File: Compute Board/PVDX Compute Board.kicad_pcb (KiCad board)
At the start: 2 copper layers, 82.5 x 82.5 mm, 84 parts, among them IC1 MCP1603-330I_MC, IC2 MCP1603-180I_MC, J1 USB_C_Receptacle_USB2.0_14P, J2 FTSH-105-01-L-DV-007-K, J3 Conn_01x02, J4 Conn_02x06_Top_Bottom, J5 Conn_02x08_Counter_Clockwise, J6 Conn_01x06, J7 Conn_01x07, J8 Conn_01x05, J9 Conn_01x08, U1 EM008LX, U10 Sen-Z-f, U11 SAMD51, U2 EM008LX, U3 EM008LX, U4 TXS0108EPW, U5 TXS0108EPW, U6 SCH16T-K01-1, U7 MagI2C, U8 Sen-XY-f, U9 Sen-XY-f

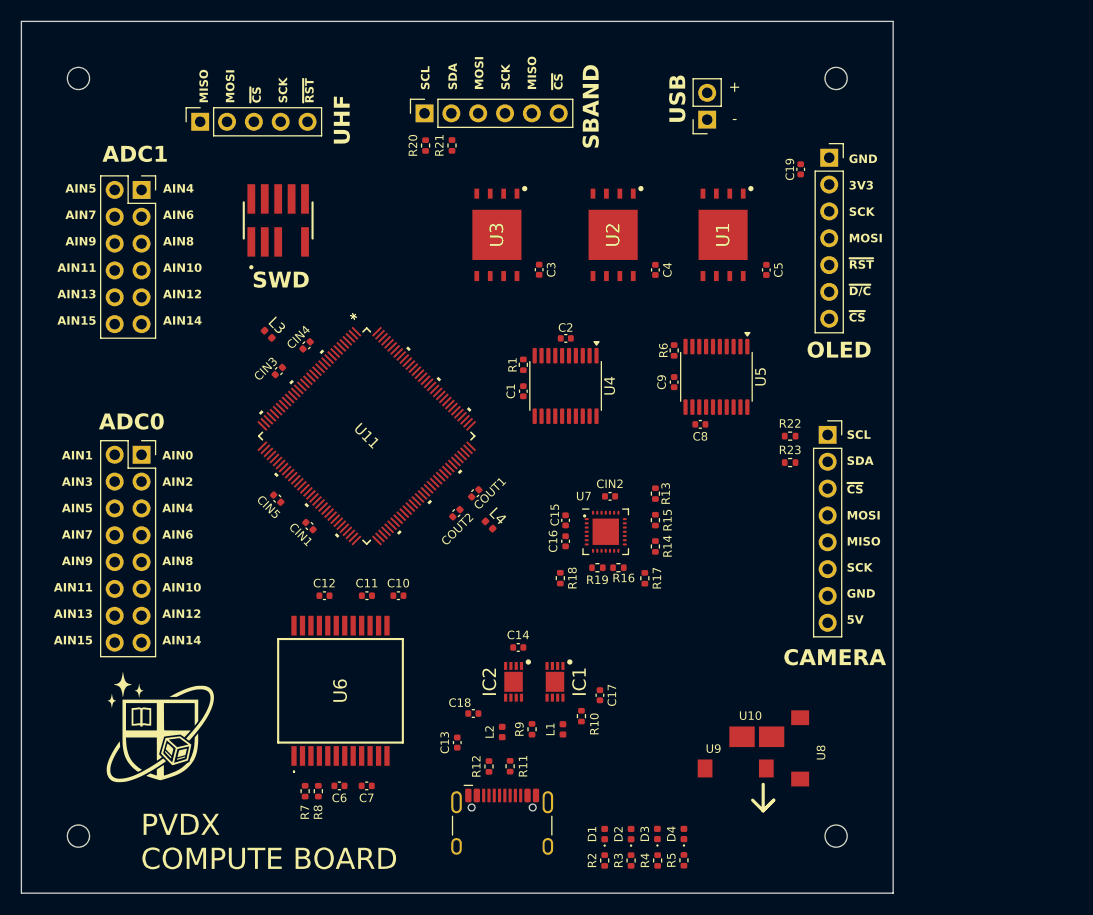
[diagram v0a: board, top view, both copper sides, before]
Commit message: Push layout-ready schematics and partial routing
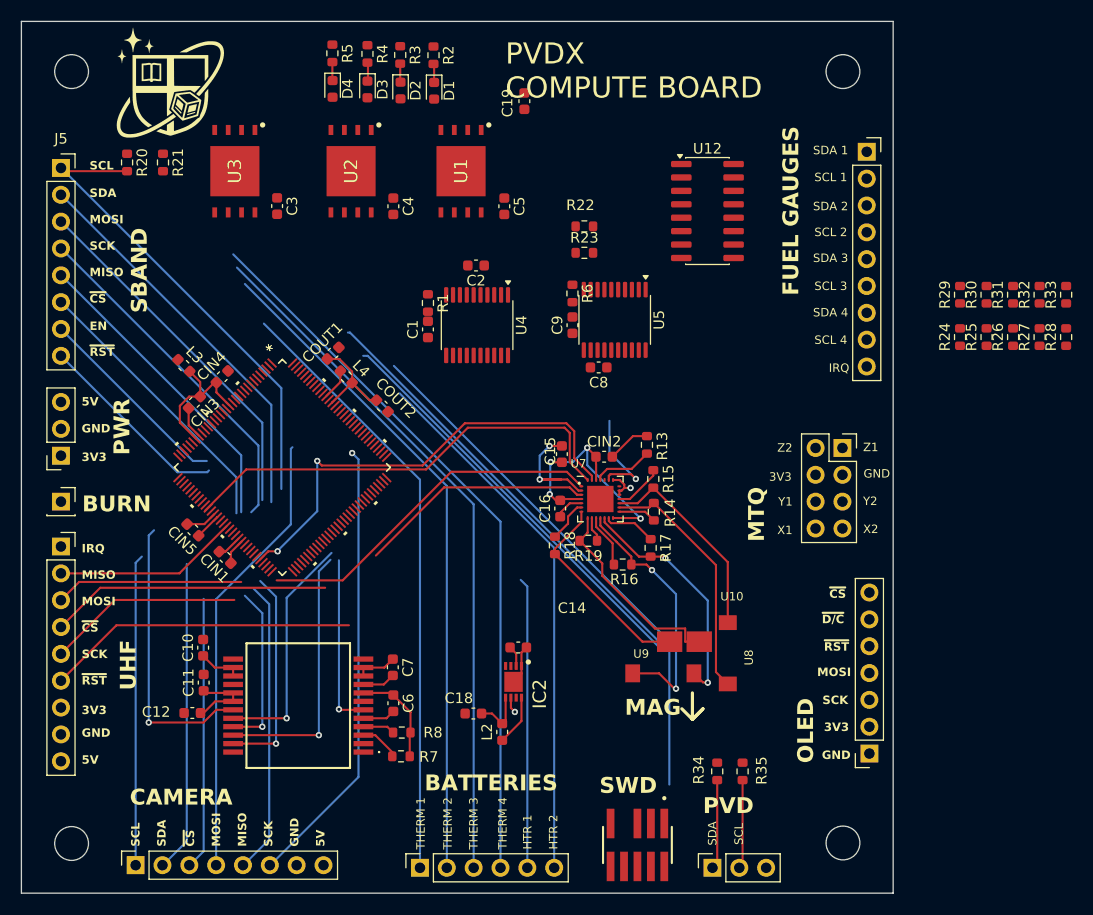
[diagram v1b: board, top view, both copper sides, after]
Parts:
- removed C13, C17: 4.7 uF, Capacitor_SMD:C_0402_1005Metric
- removed IC1: MCP1603-330I_MC, MPC1603:MPC1603-330
- removed J4: Conn_02x06_Top_Bottom, Connector_PinSocket_2.54mm:PinSocket_2x06_P2.54mm_Vertical
- removed L1: 4.7 uH, Inductor_SMD:L_0402_1005Metric
- removed R10, R9: 5.1K, Resistor_SMD:R_0402_1005Metric
- removed R11, R12: 22, Resistor_SMD:R_0402_1005Metric
- added J10: Conn_01x03, Connector_PinSocket_2.54mm:PinSocket_1x03_P2.54mm_Vertical, F.Cu at (204.4, 99.6)
- added J11: Conn_01x01, Connector_PinSocket_2.54mm:PinSocket_1x01_P2.54mm_Vertical, F.Cu at (142.7, 65.0)
- added J12: Conn_01x03, Connector_PinSocket_2.54mm:PinSocket_1x03_P2.54mm_Vertical, F.Cu at (142.7, 60.6)
- added R24: 10k, Resistor_SMD:R_0603_1608Metric, F.Cu at (227.8, 49.4)
- added R25: 10k, Resistor_SMD:R_0603_1608Metric, F.Cu at (230.3, 49.4)
- added R26: 10k, Resistor_SMD:R_0603_1608Metric, F.Cu at (232.8, 49.4)
- added R27: 10k, Resistor_SMD:R_0603_1608Metric, F.Cu at (235.4, 49.4)
- added R28: 10k, Resistor_SMD:R_0603_1608Metric, F.Cu at (237.9, 49.4)
- added R29: 10k, Resistor_SMD:R_0603_1608Metric, F.Cu at (227.8, 45.4)
- added R30: 10k, Resistor_SMD:R_0603_1608Metric, F.Cu at (230.3, 45.4)
- added R31: 10k, Resistor_SMD:R_0603_1608Metric, F.Cu at (232.8, 45.4)
- added R32: 10k, Resistor_SMD:R_0603_1608Metric, F.Cu at (235.4, 45.4)
- added R33: 10k, Resistor_SMD:R_0603_1608Metric, F.Cu at (237.9, 45.4)
- added R34: 10k, Resistor_SMD:R_0603_1608Metric, F.Cu at (204.8, 90.5)
- added R35: 10k, Resistor_SMD:R_0603_1608Metric, F.Cu at (207.2, 90.5)
- added U12: TCA9546AD, Package_SO:SOIC-16_3.9x9.9mm_P1.27mm, F.Cu at (203.9, 37.4)
- C1, C10, C11, C12, C14, C15, C16, C18, C19, C2, C3, C4, C5, C6, C7, C8, C9, CIN1, CIN2, CIN3, CIN4, CIN5, COUT1, COUT2: footprint Capacitor_SMD:C_0402_1005Metric -> Capacitor_SMD:C_0603_1608Metric
- D1, D2, D3, D4: footprint LED_SMD:LED_0402_1005Metric -> LED_SMD:LED_0603_1608Metric
- H1, H2, H3, H4: footprint MountingHole:MountingHole_2.1mm -> MountingHole:MountingHole_3.2mm_M3
- J1: value USB_C_Receptacle_USB2.0_14P -> Conn_02x04_Counter_Clockwise; footprint Connector_USB:USB_C_Receptacle_HCTL_HC-TYPE-C-16P-01A -> Connector_PinSocket_2.54mm:PinSocket_2x04_P2.54mm_Vertical
- J3: value Conn_01x02 -> Conn_01x06; footprint Connector_PinSocket_2.54mm:PinSocket_1x02_P2.54mm_Vertical -> Connector_PinSocket_2.54mm:PinSocket_1x06_P2.54mm_Vertical
- J5: value Conn_02x08_Counter_Clockwise -> Conn_01x08; footprint Connector_PinSocket_2.54mm:PinSocket_2x08_P2.54mm_Vertical -> Connector_PinSocket_2.54mm:PinSocket_1x08_P2.54mm_Vertical
- J6: value Conn_01x06 -> Conn_01x07; footprint Connector_PinSocket_2.54mm:PinSocket_1x06_P2.54mm_Vertical -> Connector_PinSocket_2.54mm:PinSocket_1x07_P2.54mm_Vertical
- J7: value Conn_01x07 -> Conn_01x09; footprint Connector_PinSocket_2.54mm:PinSocket_1x07_P2.54mm_Vertical -> Connector_PinSocket_2.54mm:PinSocket_1x09_P2.54mm_Vertical
- J8: value Conn_01x05 -> Conn_01x09; footprint Connector_PinSocket_2.54mm:PinSocket_1x05_P2.54mm_Vertical -> Connector_PinSocket_2.54mm:PinSocket_1x09_P2.54mm_Vertical
- L2, L3, L4: footprint Inductor_SMD:L_0402_1005Metric -> Inductor_SMD:L_0603_1608Metric
- R1, R13, R14, R15, R16, R17, R18, R19, R20, R21, R22, R23, R6, R7, R8: footprint Resistor_SMD:R_0402_1005Metric -> Resistor_SMD:R_0603_1608Metric
- R2, R3, R4, R5: value 1K -> 330; footprint Resistor_SMD:R_0402_1005Metric -> Resistor_SMD:R_0603_1608Metric
- moved R5 83.3 mm to (168.4, 22.5), turned to -90 degrees
- moved J7 81.5 mm to (142.7, 69.2)
- moved R4 81.1 mm to (171.8, 22.6), turned to -90 degrees
- moved R3 79.3 mm to (174.8, 22.7), turned to -90 degrees
- moved D4 78.0 mm to (168.4, 25.9), turned to -90 degrees
- moved R2 77.9 mm to (178.0, 22.7), turned to -90 degrees
- moved J9 77.1 mm to (149.8, 99.3), turned to 90 degrees
- moved J3 75.8 mm to (176.7, 99.6), turned to 90 degrees
- moved D3 75.6 mm to (171.8, 25.9), turned to -90 degrees
- moved J6 73.8 mm to (219.2, 88.8), turned to 180 degrees
- moved D2 73.7 mm to (174.9, 26.0), turned to -90 degrees
- moved D1 72.2 mm to (178.1, 26.1), turned to -90 degrees
- moved J2 68.2 mm to (197.3, 97.4), turned to 180 degrees
- moved J8 63.1 mm to (219.0, 31.8), turned to 0 degrees
- moved G*** 61.0 mm to (153.1, 25.7)
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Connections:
- C14 pad 1: +5V -> +3V3
- CIN3 pad 1: Net-(U11A-VDANA) -> VDDANA
- CIN4 pad 1: Net-(U11A-VDANA) -> VDDANA
- IC2 pad 2: +5V -> +3V3
- J3 pad 1: USB D- -> ADC1 AIN6
- J3 pad 2: USB D+ -> ADC1 AIN7
- J5 pad 1: ADC0 AIN0 -> SBAND SCL
- J5 pad 2: ADC0 AIN1 -> SBAND SDA
- J5 pad 3: ADC0 AIN2 -> SBAND MOSI
- J5 pad 4: ADC0 AIN3 -> SBAND SCK
- J5 pad 5: ADC0 AIN4 -> SBAND MISO
- J5 pad 6: ADC0 AIN5 -> SBAND ~{CS}
- J5 pad 7: ADC0 AIN6 -> SBAND EN
- J5 pad 8: ADC0 AIN7 -> SBAND ~{RST}
- J6 pad 1: SBAND SCL -> GND
- J6 pad 2: SBAND SDA -> +3V3
- J6 pad 3: SBAND MOSI -> OLED SCK
- J6 pad 4: SBAND SCK -> OLED MOSI
- J6 pad 5: SBAND MISO -> OLED ~{RST}
- J6 pad 6: SBAND ~{CS} -> OLED ~{D/C}
- J7 pad 1: GND -> UHF IRQ
- J7 pad 2: +3V3 -> UHF MISO
- J7 pad 3: OLED SCK -> UHF MOSI
- J7 pad 4: OLED MOSI -> UHF ~{CS}
- J7 pad 5: OLED ~{RST} -> UHF SCK
- J7 pad 6: OLED ~{D/C} -> UHF ~{RESET}
- J7 pad 7: OLED ~{CS} -> +3V3
- J8 pad 1: UHF MISO -> Net-(J8-Pin_1)
- J8 pad 2: UHF MOSI -> Net-(J8-Pin_2)
- J8 pad 3: UHF ~{CS} -> Net-(J8-Pin_3)
- J8 pad 4: UHF SCK -> Net-(J8-Pin_4)
- J8 pad 5: UHF ~{RESET} -> Net-(J8-Pin_5)
- L3 pad 2: Net-(U11A-VDANA) -> VDDANA
- R16 pad 2: Net-(U7-YNN) -> Net-(U7-YNP)
- U11 pad 104: unconnected-(U11C-PB28-Pad104) -> EPS IRQ
- U11 pad 106: (no net) -> GND
- U11 pad 107: (no net) -> +3V3
- U11 pad 108: unconnected-(U11D-PC24-Pad108) -> HEATER 2
- U11 pad 109: unconnected-(U11D-PC25-Pad109) -> SBAND EN
- U11 pad 110: unconnected-(U11D-PC26-Pad110) -> SBAND ~{RST}
- U11 pad 114: (no net) -> SWD ~{RESET}
- U11 pad 115: (no net) -> Net-(U11A-VDDCORE)
- U11 pad 117: (no net) -> Net-(U11A-VSW)
- U11 pad 118: (no net) -> +3V3
- U11 pad 123: ADC1 AIN12 -> unconnected-(U11D-PC30-Pad123)
- U11 pad 124: ADC1 AIN13 -> unconnected-(U11D-PC31-Pad124)
- U11 pad 13: ADC1 AIN14 -> unconnected-(U11E-PD00-Pad13)
- U11 pad 14: (no net) -> GND
- U11 pad 15: (no net) -> VDDANA
- U11 pad 16: ADC1 AIN15 -> unconnected-(U11E-PD01-Pad16)
- U11 pad 25: (no net) -> GND
- U11 pad 26: (no net) -> VDDANA
- U11 pad 3: ADC1 AIN10 -> unconnected-(U11D-PC00-Pad3)
- U11 pad 31: (no net) -> GND
- U11 pad 32: (no net) -> +3V3
- U11 pad 37: (no net) -> +3V3
- U11 pad 38: (no net) -> GND
- U11 pad 4: ADC1 AIN11 -> unconnected-(U11D-PC01-Pad4)
- U11 pad 45: (no net) -> GND
- U11 pad 46: (no net) -> +3V3
- U11 pad 5: (no net) -> GND
- U11 pad 53: (no net) -> GND
- U11 pad 54: (no net) -> +3V3
- U11 pad 6: (no net) -> VDDANA
- U11 pad 64: (no net) -> GND
- U11 pad 65: (no net) -> +3V3
- U11 pad 68: OLED MISO -> unconnected-(U11B-PA18-Pad68)
- U11 pad 77: unconnected-(U11D-PC23-Pad77) -> HEATER 1
- U11 pad 78: (no net) -> GND
- U11 pad 79: (no net) -> +3V3
- U11 pad 86: unconnected-(U11C-PB20-Pad86) -> EPS ~{RST}
- U11 pad 87: unconnected-(U11C-PB21-Pad87) -> EPS A0
- U11 pad 90: (no net) -> GND
- U11 pad 91: (no net) -> +3V3
- U11 pad 96: (no net) -> GND
- U11 pad 97: (no net) -> +3V3
- U11 pad 98: unconnected-(U11C-PB22-Pad98) -> EPS A1
- U11 pad 99: unconnected-(U11C-PB23-Pad99) -> EPS A2
- U6 pad 20: GYRO DRDY -> GYRO ~{DRDY}
- U7 pad 11: Net-(U7-YNN) -> Net-(U7-YNP)
- U7 pad 23: MAG DRDY -> MAG ~{DRDY}
- U9 pad 1: Net-(U7-YNN) -> Net-(U7-YNP)
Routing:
- net MAG/GYRO MISO: track 0.00 -> 70.0 mm, vias 0 -> 1
- net ADC1 AIN9: track 0.00 -> 68.8 mm
- net ADC1 AIN8: track 0.00 -> 66.4 mm
- net ADC1 AIN7: track 0.00 -> 63.5 mm
- net MAG/GYRO SCK: track 0.00 -> 59.9 mm, vias 0 -> 3
- net ADC1 AIN6: track 0.00 -> 57.9 mm
- net MAG/GYRO MOSI: track 0.00 -> 53.8 mm, vias 0 -> 1
- net HEATER 2: track 0.00 -> 51.3 mm
- net +3V3: track 0.00 -> 50.4 mm, vias 0 -> 4
- net SWD ~{RESET}: track 0.00 -> 50.4 mm
- net SBAND SCL: track 0.00 -> 44.6 mm
- net CAMERA SCK: track 0.00 -> 42.8 mm, vias 0 -> 1
- net CAMERA MOSI: track 0.00 -> 42.6 mm
- net SWCLK: track 0.00 -> 42.4 mm
- net GND: track 0.00 -> 39.6 mm, vias 0 -> 3
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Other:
- board text added: "BATTERIES"
- board text added: "BURN"
- board text added: "EN"
- board text added: "FUEL GAUGES"
- board text added: "HTR 1"
- board text added: "HTR 2"
- board text added: "IRQ"
- board text added: "MAG"
- board text added: "MTQ"
- board text added: "PVD"
- board text added: "PWR"
- board text added: "SCL 1"
- board text added: "SCL 2"
- board text added: "SCL 3"
- board text added: "SCL 4"
- board text added: "SDA 1"
- board text added: "SDA 2"
- board text added: "SDA 3"
- board text added: "SDA 4"
- board text added: "THERM 1"
- board text added: "THERM 2"
- board text added: "THERM 3"
- board text added: "THERM 4"
- board text added: "X1"
- board text added: "X2"
- board text added: "Y1"
- board text added: "Y2"
- board text added: "Z1"
- board text added: "Z2"
- board text removed: "+"
- board text removed: "-"
- board text removed: "ADC0"
- board text removed: "ADC1"
- board text removed: "AIN0"
- board text removed: "AIN1"
- board text removed: "AIN10"
- board text removed: "AIN11"
- board text removed: "AIN12"
- board text removed: "AIN13"
- board text removed: "AIN14"
- board text removed: "AIN15"
- board text removed: "AIN2"
- board text removed: "AIN3"
- board text removed: "AIN4"
- board text removed: "AIN5"
- board text removed: "AIN6"
- board text removed: "AIN7"
- board text removed: "AIN8"
- board text removed: "AIN9"
- board text removed: "USB"

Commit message: Push finished layout minus perovskites
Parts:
- added J13: Conn_01x18, Ribbon cables:FH34SRJ18S05SH50, F.Cu at (156.5, 23.8)
- moved C19 70.2 mm to (215.7, 90.9), turned to 180 degrees
- moved R22 66.6 mm to (149.7, 90.1), turned to -90 degrees
- moved R23 63.2 mm to (152.0, 90.1), turned to -90 degrees
- moved G*** 46.7 mm to (199.3, 32.4)
- moved R33 32.4 mm to (205.8, 50.0), turned to -90 degrees
- moved R32 31.7 mm to (204.0, 50.0), turned to -90 degrees
- moved R28 31.4 mm to (209.4, 36.2), turned to 0 degrees
- moved R27 28.3 mm to (209.4, 38.0), turned to 0 degrees
- moved R31 27.6 mm to (209.4, 30.8), turned to 0 degrees
- moved R26 25.3 mm to (209.4, 39.8), turned to 0 degrees
- moved R30 24.5 mm to (209.4, 32.6), turned to 0 degrees
- moved R25 22.3 mm to (209.4, 41.6), turned to 0 degrees
- moved R29 21.4 mm to (209.4, 34.4), turned to 0 degrees
- moved R24 19.4 mm to (209.4, 43.4), turned to 0 degrees
- moved U12 18.8 mm to (207.5, 56.0), turned to 90 degrees
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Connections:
- R34 pad 1: unconnected-(R34-Pad1) -> +3V3
- R35 pad 1: unconnected-(R35-Pad1) -> +3V3
- U11 pad 116: (no net) -> GND
- U12 pad 16: unconnected-(U12-VCC-Pad16) -> +5V
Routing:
- net +3V3: track 50.4 -> 445.5 mm, vias 4 -> 41
- net GND: track 39.6 -> 401.2 mm, vias 3 -> 52
- net +5V: track 1.51 -> 204.5 mm, vias 1 -> 5
- net +1V8: track 4.95 -> 124.0 mm, vias 0 -> 14
- net MRAM 3 ~{WP}: track 0.00 -> 103.1 mm, vias 0 -> 4
- net MRAM 3 ~{RESET}: track 0.00 -> 101.3 mm, vias 0 -> 2
- net MRAM 3 ~{CS}: track 0.00 -> 97.6 mm, vias 0 -> 4
- net OLED ~{D/C}: track 0.00 -> 85.7 mm, vias 0 -> 2
- net OLED ~{RST}: track 0.00 -> 84.8 mm, vias 0 -> 2
- net OLED SCK: track 0.00 -> 84.3 mm, vias 0 -> 1
- net OLED MOSI: track 0.00 -> 82.6 mm, vias 0 -> 1
- net MAG ~{DRDY}: track 9.74 -> 90.6 mm, vias 1 -> 6
- net OLED ~{CS}: track 0.00 -> 74.0 mm, vias 0 -> 2
- net MRAM 2 ~{CS}: track 0.00 -> 66.9 mm, vias 0 -> 2
- net LED ~{RED}: track 0.00 -> 63.0 mm, vias 0 -> 2
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- added copper zone on F.Cu, net +3V3
- added copper zone on B.Cu, net GND

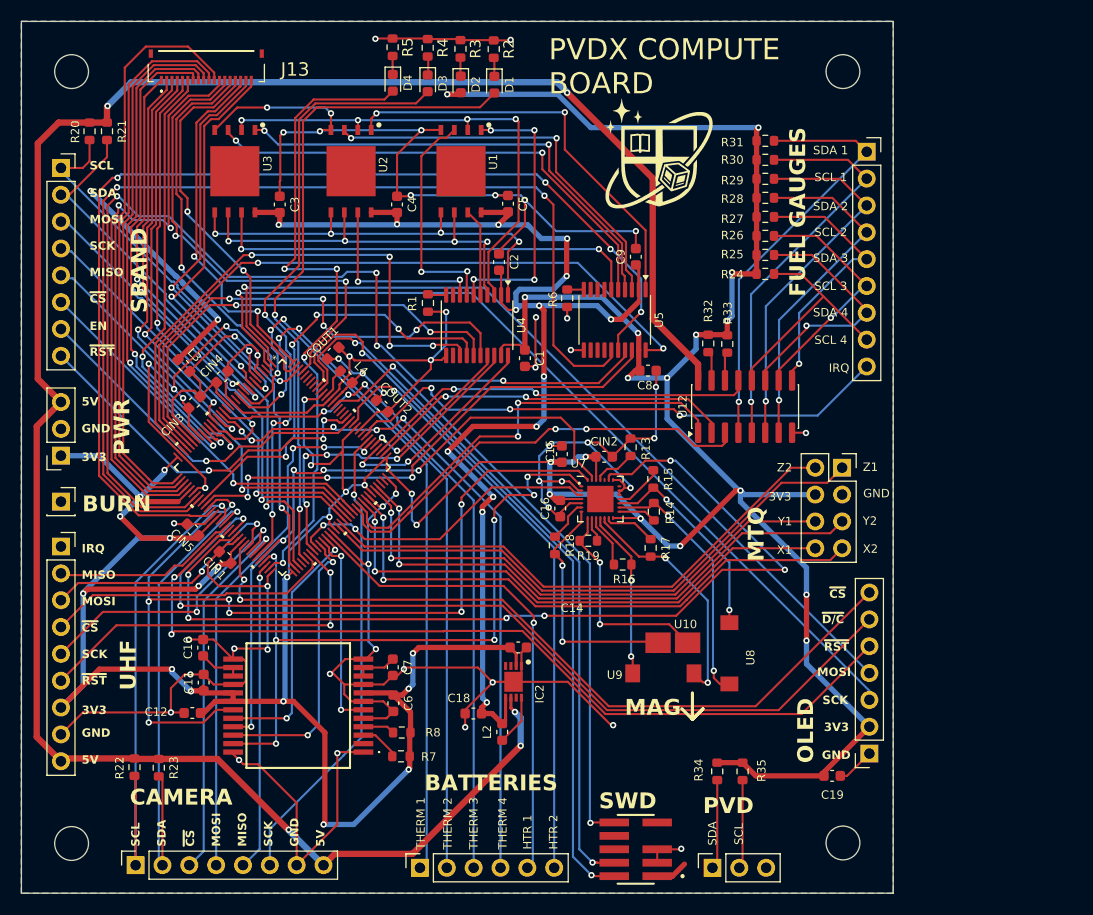
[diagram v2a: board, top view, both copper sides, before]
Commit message: Add perovskite and magnetorquer sleep routing
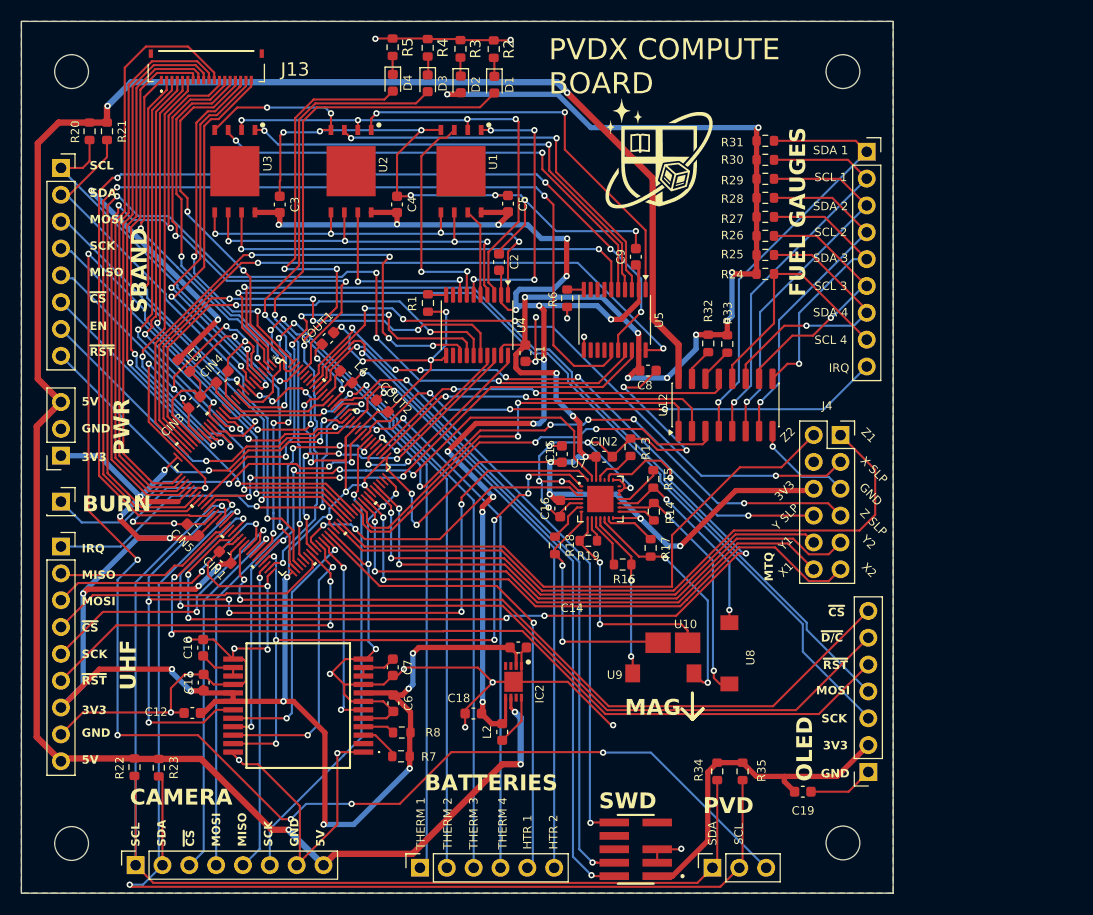
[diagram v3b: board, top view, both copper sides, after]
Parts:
- removed J1: Conn_02x04_Counter_Clockwise, Connector_PinSocket_2.54mm:PinSocket_2x04_P2.54mm_Vertical
- added J4: Conn_02x06_Counter_Clockwise, Connector_PinSocket_2.54mm:PinSocket_2x06_P2.54mm_Vertical, F.Cu at (216.5, 58.6)
- moved C19 3.15 mm to (212.9, 92.4)
- moved U12 1.86 mm to (205.6, 55.8)
- moved J6 1.74 mm to (219.2, 90.5)
- moved COUT1 1.49 mm to (168.0, 49.5)
- moved C1 0.48 mm to (186.7, 50.9)
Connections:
- J10 pad 1: Net-(J10-Pin_1) -> CAMERA/PVD SCL
- J10 pad 2: Net-(J10-Pin_2) -> CAMERA/PVD SDA
- J10 pad 3: unconnected-(J10-Pin_3-Pad3) -> PVD DAC
- J9 pad 1: CAMERA SCL -> CAMERA/PVD SCL
- J9 pad 2: CAMERA SDA -> CAMERA/PVD SDA
- R22 pad 2: CAMERA SCL -> CAMERA/PVD SCL
- R23 pad 2: CAMERA SDA -> CAMERA/PVD SDA
- R34 pad 2: Net-(J10-Pin_1) -> CAMERA/PVD SCL
- R35 pad 2: Net-(J10-Pin_2) -> CAMERA/PVD SDA
- U11 pad 105: unconnected-(U11C-PB29-Pad105) -> BURN CTRL
- U11 pad 111: unconnected-(U11D-PC27-Pad111) -> MTQ_Z_SLP
- U11 pad 113: unconnected-(U11B-PA27-Pad113) -> UHF IRQ
- U11 pad 121: unconnected-(U11C-PB30-Pad121) -> MTQ_X_SLP
- U11 pad 122: unconnected-(U11C-PB31-Pad122) -> MTQ_Y_SLP
- U11 pad 3: unconnected-(U11D-PC00-Pad3) -> ADC0 AIN0
- U11 pad 47: CAMERA SCL -> CAMERA/PVD SCL
- U11 pad 48: CAMERA SDA -> CAMERA/PVD SDA
- U11 pad 9: ADC0 AIN0 -> PVD DAC
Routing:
- net PVD DAC: track 0.00 -> 158.7 mm, vias 0 -> 11
- net CAMERA/PVD SDA: track 0.00 -> 117.3 mm, vias 0 -> 2
- net CAMERA/PVD SCL: track 0.00 -> 111.7 mm, vias 0 -> 1
- net MTQ_X_SLP: track 0.00 -> 61.3 mm, vias 0 -> 4
- net MTQ_Y_SLP: track 0.00 -> 58.5 mm, vias 0 -> 6
- net MTQ_Z_SLP: track 0.00 -> 57.9 mm, vias 0 -> 6
- net CAMERA SCL: track 48.0 -> 0.00 mm, vias 1 -> 0
- net CAMERA SDA: track 46.9 -> 0.00 mm, vias 1 -> 0
- net UHF IRQ: track 0.00 -> 41.6 mm, vias 0 -> 3
- net BURN CTRL: track 0.00 -> 34.6 mm, vias 0 -> 3
- net GND: track 401.2 -> 428.8 mm, vias 52 -> 54
- net +3V3: track 445.5 -> 432.4 mm, vias 41 -> 40
- net MTQ_Z_IN1: track 55.0 -> 65.2 mm
- net Net-(J10-Pin_2): track 7.99 -> 0.00 mm
- net Net-(J10-Pin_1): track 7.85 -> 0.00 mm
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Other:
- board text added: "X SLP"
- board text added: "Y SLP"
- board text added: "Z SLP"

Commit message: Finished routing
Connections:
- J10 pad 1: CAMERA/PVD SCL -> CAMERA/PVD/EPS SCL
- J10 pad 2: CAMERA/PVD SDA -> CAMERA/PVD/EPS SDA
- J9 pad 1: CAMERA/PVD SCL -> CAMERA/PVD/EPS SCL
- J9 pad 2: CAMERA/PVD SDA -> CAMERA/PVD/EPS SDA
- R22 pad 2: CAMERA/PVD SCL -> CAMERA/PVD/EPS SCL
- R23 pad 2: CAMERA/PVD SDA -> CAMERA/PVD/EPS SDA
- R32 pad 2: EPS SDA -> CAMERA/PVD/EPS SCL
- R33 pad 2: EPS SCL -> CAMERA/PVD/EPS SDA
- R34 pad 2: CAMERA/PVD SCL -> CAMERA/PVD/EPS SCL
- R35 pad 2: CAMERA/PVD SDA -> CAMERA/PVD/EPS SDA
- U11 pad 47: CAMERA/PVD SCL -> CAMERA/PVD/EPS SCL
- U11 pad 48: CAMERA/PVD SDA -> CAMERA/PVD/EPS SDA
- U12 pad 14: EPS SCL -> CAMERA/PVD/EPS SDA
- U12 pad 15: EPS SDA -> CAMERA/PVD/EPS SCL
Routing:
- net CAMERA/PVD/EPS SDA: track 0.00 -> 165.7 mm, vias 0 -> 4
- net CAMERA/PVD/EPS SCL: track 0.00 -> 161.0 mm, vias 0 -> 5
- net CAMERA/PVD SDA: track 117.3 -> 0.00 mm, vias 2 -> 0
- net CAMERA/PVD SCL: track 111.7 -> 0.00 mm, vias 1 -> 0
- net EPS SDA: track 3.16 -> 0.00 mm
- net EPS SCL: track 2.92 -> 0.00 mm
- net EPS A2: track 35.7 -> 35.9 mm, vias 2 -> 4
